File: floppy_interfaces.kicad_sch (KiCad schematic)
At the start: 24 parts, among them J13 Conn_01x04_Male, J14 Conn_02x17_Odd_Even, J16 Conn_01x04_Male, J6 SDF-60J for IEC 1541 serial p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, U1 74LS373, U2 74LVC374, U22 74LS06N, U3 74LVC374, U4 74LS373

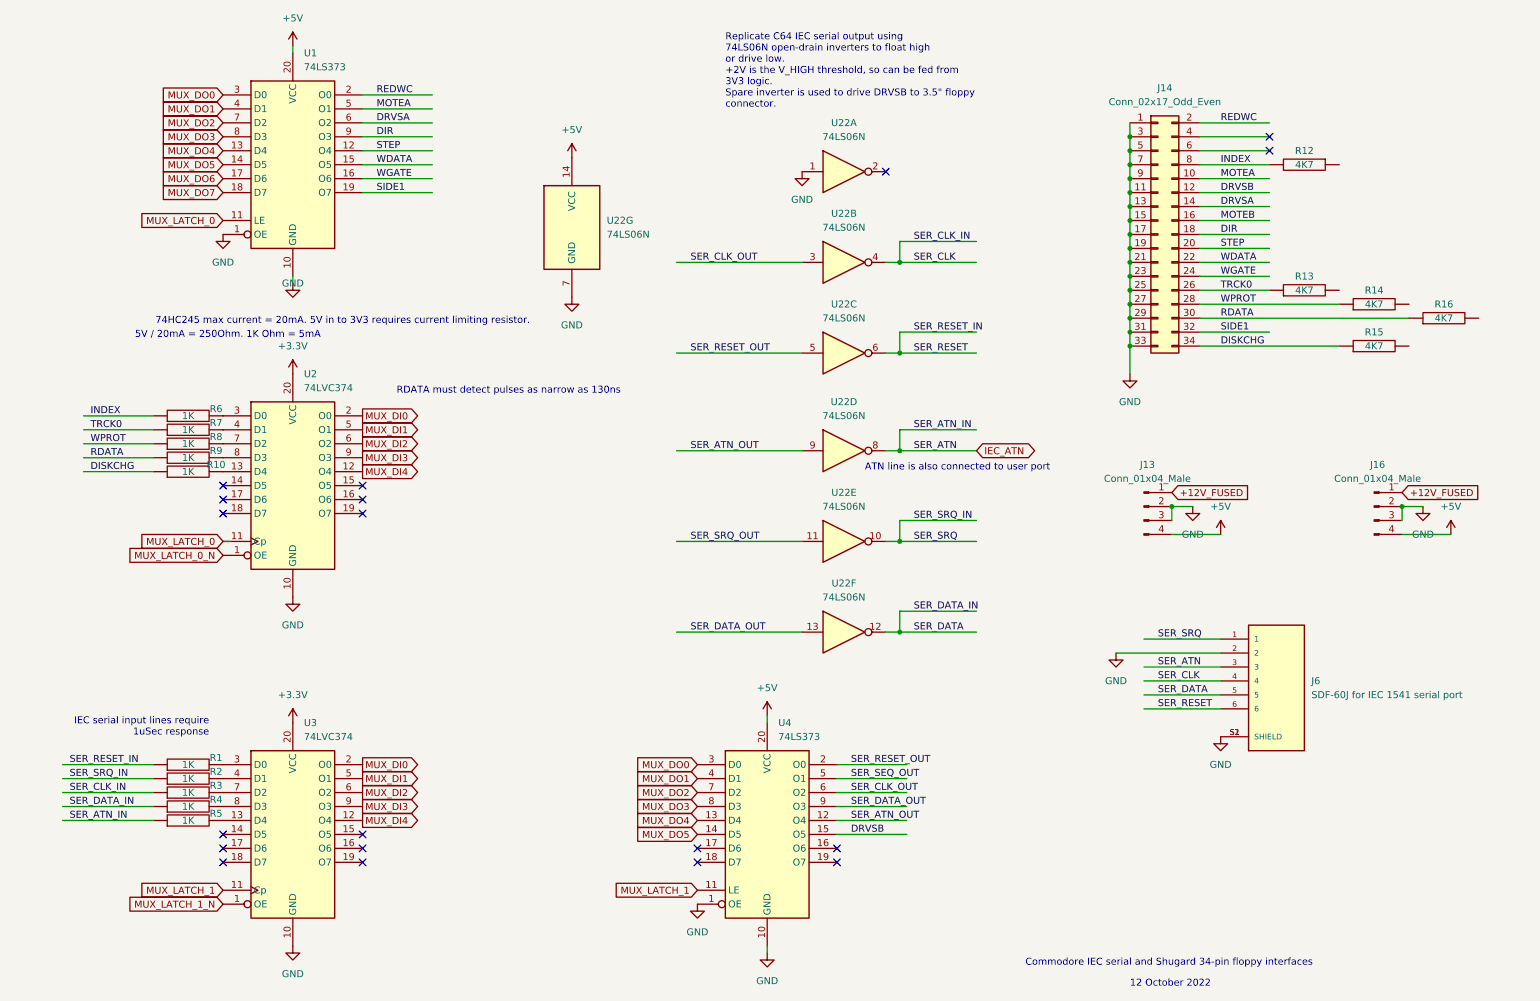
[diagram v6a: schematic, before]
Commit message: replace remaining 74LS373 with 74LS374s #5
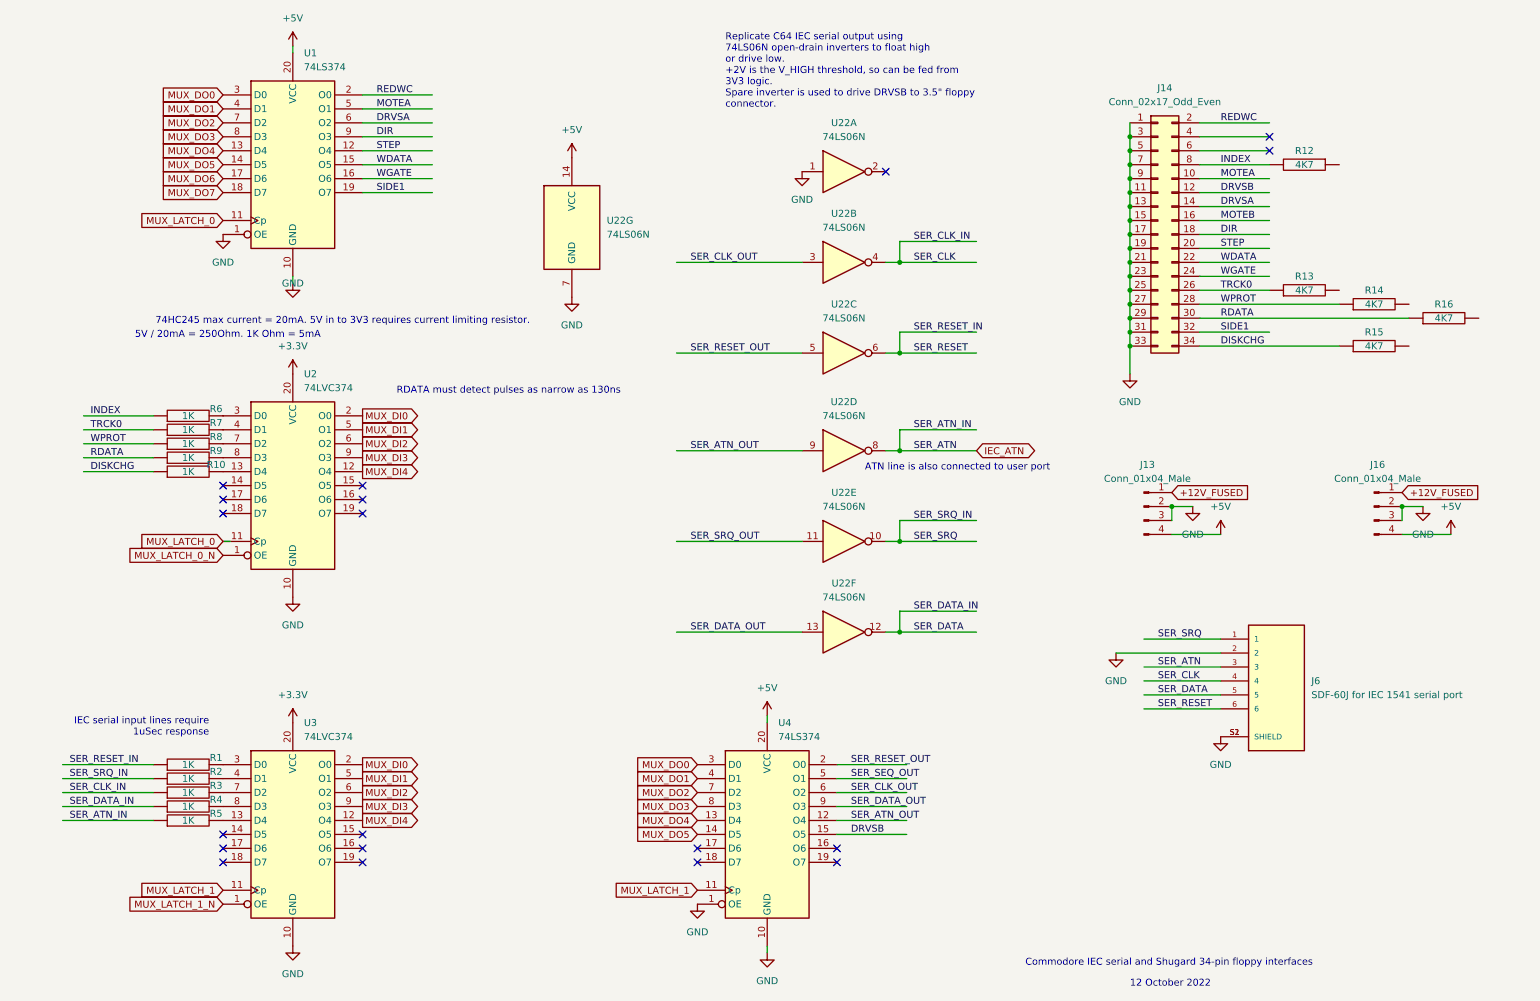
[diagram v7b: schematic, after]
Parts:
- removed U1, U4: 74LS373, Package_DIP:DIP-20_W7.62mm, symbol 74xx:74LS373
- added U1, U4: 74LS374, Package_DIP:DIP-20_W7.62mm, symbol 74xx:74LS374
- J13, J16: footprint PinHeader_1x04_P2.54mm_Vertical -> Connector_PinHeader_2.54mm:PinHeader_1x04_P2.54mm_Vertical
- J6: footprint CUI_SDF-60J -> snapeda:CUI_SDF-60J
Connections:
- net +5V: now also U1.20 (VCC), U4.20 (VCC)
- net DIR: now also U1.9 (O3)
- net DRVSA: now also U1.6 (O2)
- net DRVSB: now also U4.15 (O5)
- net GND: now also U1.1 (OE), U1.10 (GND), U4.1 (OE), U4.10 (GND)
- net MOTEA: now also U1.5 (O1)
- net MUX_DO0: now also U1.3 (D0), U4.3 (D0)
- net MUX_DO1: now also U1.4 (D1), U4.4 (D1)
- net MUX_DO2: now also U1.7 (D2), U4.7 (D2)
- net MUX_DO3: now also U1.8 (D3), U4.8 (D3)
- net MUX_DO4: now also U1.13 (D4), U4.13 (D4)
- net MUX_DO5: now also U1.14 (D5), U4.14 (D5)
- net MUX_DO6: now also U1.17 (D6)
- net MUX_DO7: now also U1.18 (D7)
- net MUX_LATCH_0: now also U1.11 (Cp)
- net MUX_LATCH_1: now also U4.11 (Cp)
- net REDWC: now also U1.2 (O0)
- net SER_ATN_OUT: now also U4.12 (O4)
- net SER_CLK_OUT: now also U4.6 (O2)
- net SER_DATA_OUT: now also U4.9 (O3)
- net SER_RESET_OUT: now also U4.2 (O0)
- net SER_SEQ_OUT: now also U4.5 (O1)
- net SIDE1: now also U1.19 (O7)
- net STEP: now also U1.12 (O4)
- net WDATA: now also U1.15 (O5)
- net WGATE: now also U1.16 (O6)

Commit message: make R/W signals on cart port open-collector with pullup #6
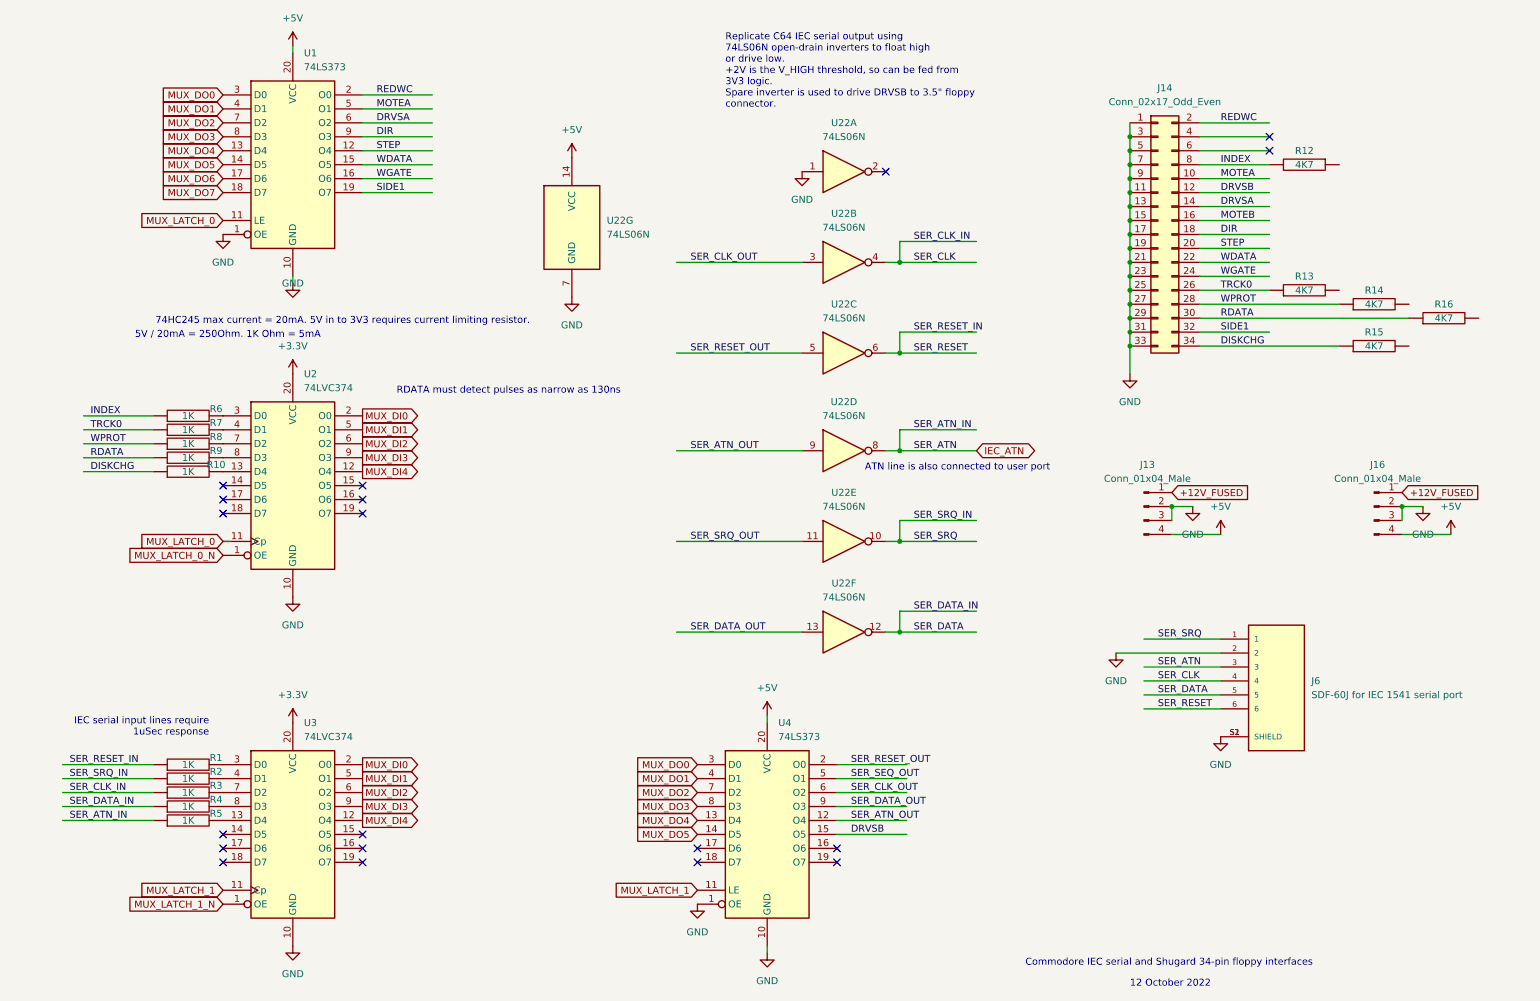
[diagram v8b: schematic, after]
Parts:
- removed U1, U4: 74LS374, Package_DIP:DIP-20_W7.62mm, symbol 74xx:74LS374
- added U1, U4: 74LS373, Package_DIP:DIP-20_W7.62mm, symbol 74xx:74LS373
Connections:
- net +5V: now also U1.20 (VCC), U4.20 (VCC)
- net DIR: now also U1.9 (O3)
- net DRVSA: now also U1.6 (O2)
- net DRVSB: now also U4.15 (O5)
- net GND: now also U1.1 (OE), U1.10 (GND), U4.1 (OE), U4.10 (GND)
- net MOTEA: now also U1.5 (O1)
- net MUX_DO0: now also U1.3 (D0), U4.3 (D0)
- net MUX_DO1: now also U1.4 (D1), U4.4 (D1)
- net MUX_DO2: now also U1.7 (D2), U4.7 (D2)
- net MUX_DO3: now also U1.8 (D3), U4.8 (D3)
- net MUX_DO4: now also U1.13 (D4), U4.13 (D4)
- net MUX_DO5: now also U1.14 (D5), U4.14 (D5)
- net MUX_DO6: now also U1.17 (D6)
- net MUX_DO7: now also U1.18 (D7)
- net MUX_LATCH_0: now also U1.11 (LE)
- net MUX_LATCH_1: now also U4.11 (LE)
- net REDWC: now also U1.2 (O0)
- net SER_ATN_OUT: now also U4.12 (O4)
- net SER_CLK_OUT: now also U4.6 (O2)
- net SER_DATA_OUT: now also U4.9 (O3)
- net SER_RESET_OUT: now also U4.2 (O0)
- net SER_SEQ_OUT: now also U4.5 (O1)
- net SIDE1: now also U1.19 (O7)
- net STEP: now also U1.12 (O4)
- net WDATA: now also U1.15 (O5)
- net WGATE: now also U1.16 (O6)
